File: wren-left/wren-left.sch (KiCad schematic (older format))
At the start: 65 parts, among them J1 TRRS_Jack, SW0 Reset, U1 ProMicro

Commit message: Finish Left-Hand Schematic
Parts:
- added D31, D32, D33, D34, D35, D36, D37, D38, D39, D40, D41, D42, D43, D44: D_Small, Diode_SMD:D_SOD-123, symbol Device:D_Small
- added MX31, MX32, MX33, MX34, MX35, MX36, MX37, MX38, MX39, MX40, MX42, MX43, MX44: MX-NoLED, MX_Only:MX-1U, symbol MX_Alps_Hybrid:MX-NoLED
- added MX41: MX-NoLED, MX_Only:MX-1.5U, symbol MX_Alps_Hybrid:MX-NoLED
- D1, D10, D11, D12, D13, D14, D15, D16, D17, D18, D19, D2, D20, D21, D22, D23, D24, D25, D26, D27, D28, D29, D3, D30, D4, D5, D6, D7, D8, D9: renamed from D?; footprint (none) -> Diode_SMD:D_SOD-123
- J1: footprint (none) -> footprints:TRRS_JACK_MJ4PP9
- MX1, MX10, MX11, MX12, MX13, MX14, MX15, MX16, MX17, MX18, MX19, MX2, MX20, MX21, MX22, MX23, MX24, MX25, MX26, MX27, MX28, MX29, MX3, MX30, MX4, MX5, MX6, MX7, MX8, MX9: renamed from MX?; footprint (none) -> MX_Only:MX-1U
- R1, R2: footprint (none) -> Resistor_SMD:R_0805_2012Metric
- SW0: footprint (none) -> random-keyboard-parts:SKQG-1155865
- U1: footprint (none) -> footprints:ARDUINO_PRO_MICRO
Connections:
- net COL8: now reaches U1.1 (TX(PD3))
- net COL8: now also MX19.1 (COL), MX29.1 (COL), MX9.1 (COL), MX39.1 (COL)
- net ROW3: now reaches U1.10 (D7(PE6))
- net ROW3: now also D31.1 (K), D32.1 (K), D33.1 (K), D34.1 (K), D35.1 (K), D36.1 (K), D37.1 (K), D38.1 (K), D39.1 (K), D40.1 (K)
- net ROW4: now reaches U1.11 (D8(PB4))
- net ROW4: now also D41.1 (K), D42.1 (K), D43.1 (K), D44.1 (K)
- net COL7: now reaches U1.13 (D10(PB6))
- net COL7: now also MX18.1 (COL), MX28.1 (COL), MX8.1 (COL), MX38.1 (COL)
- net COL6: now reaches U1.14 (D16(PB2))
- net COL6: now also MX17.1 (COL), MX27.1 (COL), MX7.1 (COL), MX37.1 (COL)
- net COL5: now reaches U1.15 (D14(PB3))
- net COL5: now also MX16.1 (COL), MX26.1 (COL), MX6.1 (COL), MX36.1 (COL)
- net COL4: now reaches U1.16 (D15(PB1))
- net COL4: now also MX15.1 (COL), MX25.1 (COL), MX5.1 (COL), MX35.1 (COL)
- net COL3: now reaches U1.17 (A0(PF7))
- net COL3: now also MX14.1 (COL), MX24.1 (COL), MX4.1 (COL), MX34.1 (COL), MX44.1 (COL)
- net COL2: now reaches U1.18 (A1(PF6))
- net COL2: now also MX13.1 (COL), MX23.1 (COL), MX3.1 (COL), MX33.1 (COL), MX43.1 (COL)
- net COL1: now reaches U1.19 (A2(PF5))
- net COL1: now also MX12.1 (COL), MX2.1 (COL), MX22.1 (COL), MX32.1 (COL), MX42.1 (COL)
- net COL9: now reaches U1.2 (RX(PD2))
- net COL9: now also MX10.1 (COL), MX20.1 (COL), MX30.1 (COL), MX40.1 (COL)
- net COL0: now reaches U1.20 (A3(PF4))
- net COL0: now also MX1.1 (COL), MX11.1 (COL), MX21.1 (COL), MX31.1 (COL), MX41.1 (COL)
- net ROW0: now reaches U1.7 (D4(PD4))
- net ROW0: now also D1.1 (K), D10.1 (K), D2.1 (K), D3.1 (K), D4.1 (K), D5.1 (K), D6.1 (K), D7.1 (K), D8.1 (K), D9.1 (K)
- net ROW1: now reaches U1.8 (D5(PC6))
- net ROW1: now also D11.1 (K), D12.1 (K), D13.1 (K), D14.1 (K), D15.1 (K), D16.1 (K), D17.1 (K), D18.1 (K), D19.1 (K), D20.1 (K)
- net ROW2: now reaches U1.9 (D6(PD7))
- net ROW2: now also D21.1 (K), D22.1 (K), D23.1 (K), D24.1 (K), D25.1 (K), D26.1 (K), D27.1 (K), D28.1 (K), D29.1 (K), D30.1 (K)
- net at MX1.2 (ROW): now also D1.2 (A)
- net at MX2.2 (ROW): now also D2.2 (A)
- net at D3.2 (A): now also MX3.2 (ROW)
- net at D4.2 (A): now also MX4.2 (ROW)
- net at D5.2 (A): now also MX5.2 (ROW)
- net at D6.2 (A): now also MX6.2 (ROW)
- net at D7.2 (A): now also MX7.2 (ROW)
- net at D8.2 (A): now also MX8.2 (ROW)
- net at D9.2 (A): now also MX9.2 (ROW)
- net at MX10.2 (ROW): now also D10.2 (A)
- net at MX11.2 (ROW): now also D11.2 (A)
- net at MX12.2 (ROW): now also D12.2 (A)
- net at MX13.2 (ROW): now also D13.2 (A)
- net at MX14.2 (ROW): now also D14.2 (A)
- net at MX15.2 (ROW): now also D15.2 (A)
- net at MX16.2 (ROW): now also D16.2 (A)
- net at MX17.2 (ROW): now also D17.2 (A)
- net at MX18.2 (ROW): now also D18.2 (A)
- net at MX19.2 (ROW): now also D19.2 (A)
- net at MX20.2 (ROW): now also D20.2 (A)
- net at MX21.2 (ROW): now also D21.2 (A)
- net at MX22.2 (ROW): now also D22.2 (A)
- net at MX23.2 (ROW): now also D23.2 (A)
- net at MX24.2 (ROW): now also D24.2 (A)
- net at MX25.2 (ROW): now also D25.2 (A)
- net at MX26.2 (ROW): now also D26.2 (A)
- net at MX27.2 (ROW): now also D27.2 (A)
- net at MX28.2 (ROW): now also D28.2 (A)
- net at MX29.2 (ROW): now also D29.2 (A)
- net at MX30.2 (ROW): now also D30.2 (A)
- new net: D31.2 (A), MX31.2 (ROW)
- new net: D32.2 (A), MX32.2 (ROW)
- new net: D33.2 (A), MX33.2 (ROW)
- new net: D34.2 (A), MX34.2 (ROW)
- new net: D35.2 (A), MX35.2 (ROW)
- new net: D36.2 (A), MX36.2 (ROW)
- new net: D37.2 (A), MX37.2 (ROW)
- new net: D38.2 (A), MX38.2 (ROW)
- new net: D39.2 (A), MX39.2 (ROW)
- new net: D40.2 (A), MX40.2 (ROW)
- new net: D41.2 (A), MX41.2 (ROW)
- new net: D42.2 (A), MX42.2 (ROW)
- new net: D43.2 (A), MX43.2 (ROW)
- new net: D44.2 (A), MX44.2 (ROW)
- no-connect marks 0 -> 1
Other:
- moved on the sheet: D1, D10, D11, D12, D13, D14, D15, D16, D17, D18, D19, D2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

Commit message: Routing Half-Finished
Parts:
- J1: footprint footprints:TRRS_JACK_MJ4PP9 -> Connector_Audio:Jack_3.5mm_PJ320E_Horizontal
- MX41: footprint MX_Only:MX-1.5U -> MX_Only:MX-2U-FLIPPED-ReversedStabilizers
- SW0: footprint random-keyboard-parts:SKQG-1155865 -> Button_Switch_THT:SW_PUSH_6mm
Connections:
- net COL0: now also U1.13 (D10(PB6)); no longer U1.20 (A3(PF4))
- net COL1: now also U1.14 (D16(PB2)); no longer U1.19 (A2(PF5))
- net COL2: now also U1.15 (D14(PB3)); no longer U1.18 (A1(PF6))
- net COL3: now also U1.16 (D15(PB1)); no longer U1.17 (A0(PF7))
- net COL4: now also U1.17 (A0(PF7)); no longer U1.16 (D15(PB1))
- net COL5: now also U1.18 (A1(PF6)); no longer U1.15 (D14(PB3))
- net COL6: now also U1.19 (A2(PF5)); no longer U1.14 (D16(PB2))
- net COL7: now also U1.20 (A3(PF4)); no longer U1.13 (D10(PB6))
- net COL8: now also U1.2 (RX(PD2)); no longer U1.1 (TX(PD3))
- net COL9: now also U1.1 (TX(PD3)); no longer U1.2 (RX(PD2))
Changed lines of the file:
@@
 F 0 "J1" H 2607 4675 50  0000 C CNN
 F 1 "TRRS_Jack" H 2607 4584 50  0000 C CNN
-F 2 "footprints:TRRS_JACK_MJ4PP9" H 2650 4350 50  0001 C CNN
+F 2 "Connector_Audio:Jack_3.5mm_PJ320E_Horizontal" H 2650 4350 50  0001 C CNN
 F 3 "~" H 2650 4350 50  0001 C CNN
 	1    2650 4350
@@
 F 0 "SW0" H 3750 3135 50  0000 C CNN
 F 1 "Reset" H 3750 3044 50  0000 C CNN
-F 2 "random-keyboard-parts:SKQG-1155865" H 3750 3050 50  0001 C CNN
+F 2 "Button_Switch_THT:SW_PUSH_6mm" H 3750 3050 50  0001 C CNN
 F 3 "~" H 3750 3050 50  0001 C CNN
 	1    3750 2850
@@
 F 0 "MX41" H 5133 5773 60  0000 C CNN
 F 1 "MX-NoLED" H 5133 5699 20  0000 C CNN
-F 2 "MX_Only:MX-1.5U" H 4475 5525 60  0001 C CNN
+F 2 "MX_Only:MX-2U-FLIPPED-ReversedStabilizers" H 4475 5525 60  0001 C CNN
 F 3 "" H 4475 5525 60  0001 C CNN
 	1    5100 5550
@@
 Text GLabel 9750 2350 1    50   Input ~ 0
 COL9
+Text GLabel 3250 3750 2    50   Input ~ 0
+COL0
+Text GLabel 3250 3650 2    50   Input ~ 0
+COL1
+Text GLabel 3250 3550 2    50   Input ~ 0
+COL2
+Text GLabel 3250 3450 2    50   Input ~ 0
+COL3
+Text GLabel 3250 3350 2    50   Input ~ 0
+COL4
+Text GLabel 3250 3250 2    50   Input ~ 0
+COL5
+Text GLabel 3250 3150 2    50   Input ~ 0
+COL6
 Text GLabel 3250 3050 2    50   Input ~ 0
-COL0
-Text GLabel 3250 3150 2    50   Input ~ 0
-COL1
-Text GLabel 3250 3250 2    50   Input ~ 0
-COL2
-Text GLabel 3250 3350 2    50   Input ~ 0
-COL3
-Text GLabel 3250 3450 2    50   Input ~ 0
-COL4
-Text GLabel 3250 3550 2    50   Input ~ 0
-COL5
-Text GLabel 3250 3650 2    50   Input ~ 0
-COL6
-Text GLabel 3250 3750 2    50   Input ~ 0
 COL7
+Text GLabel 1950 2750 0    50   Input ~ 0
+COL8
 Text GLabel 1950 2650 0    50   Input ~ 0
-COL8
-Text GLabel 1950 2750 0    50   Input ~ 0
 COL9
 Text GLabel 1950 3250 0    50   Input ~ 0

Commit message: Tracks Finished
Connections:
- net COL8: now also U1.9 (D6(PD7)); no longer U1.2 (RX(PD2))
- net COL9: now also U1.10 (D7(PE6)); no longer U1.1 (TX(PD3))
- net ROW0: now also U1.1 (TX(PD3)); no longer U1.7 (D4(PD4))
- net ROW1: now also U1.2 (RX(PD2)); no longer U1.8 (D5(PC6))
- net ROW2: now also U1.7 (D4(PD4)); no longer U1.9 (D6(PD7))
- net ROW3: now also U1.8 (D5(PC6)); no longer U1.10 (D7(PE6))
- net ROW4: now also U1.12 (D9(PB5)); no longer U1.11 (D8(PB4))
- no-connect marks 1 -> 2
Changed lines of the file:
@@
 Text GLabel 1950 3150 0    50   BiDi ~ 0
-SCL
-Text GLabel 3950 4250 2    50   BiDi ~ 0
-SDA
-Text GLabel 3950 4350 2    50   BiDi ~ 0
 SCL
 Text GLabel 3250 2950 2    50   Output ~ 0
@@
 F 3 "~" H 3000 4350 50  0001 C CNN
 	1    3000 4350
-	1    0    0    -1
-$EndComp
-$Comp
-L Device:R_Small R2
-U 1 1 6072E460
-P 3500 4450
-F 0 "R2" H 3559 4496 50  0000 L CNN
-F 1 "10kOhms" H 3559 4405 50  0000 L CNN
-F 2 "Resistor_SMD:R_0805_2012Metric" H 3500 4450 50  0001 C CNN
-F 3 "~" H 3500 4450 50  0001 C CNN
-	1    3500 4450
 	1    0    0    -1
 $EndComp
@@
 Text GLabel 3250 3050 2    50   Input ~ 0
 COL7
+Text GLabel 1950 3450 0    50   Input ~ 0
+COL8
+Text GLabel 1950 3550 0    50   Input ~ 0
+COL9
+Text GLabel 1950 2650 0    50   Input ~ 0
+ROW0
 Text GLabel 1950 2750 0    50   Input ~ 0
-COL8
-Text GLabel 1950 2650 0    50   Input ~ 0
-COL9
+ROW1
 Text GLabel 1950 3250 0    50   Input ~ 0
-ROW0
+ROW2
 Text GLabel 1950 3350 0    50   Input ~ 0
-ROW1
-Text GLabel 1950 3450 0    50   Input ~ 0
-ROW2
-Text GLabel 1950 3550 0    50   Input ~ 0
 ROW3
-Text GLabel 1950 3650 0    50   Input ~ 0
+Text GLabel 1950 3750 0    50   Input ~ 0
 ROW4
-NoConn ~ 1950 3750
+NoConn ~ 1950 3650
+NoConn ~ 1850 4650
+$Comp
+L Device:R_Small R2
+U 1 1 6072E460
+P 3500 4450
+F 0 "R2" H 3559 4496 50  0000 L CNN
+F 1 "10kOhms" H 3559 4405 50  0000 L CNN
+F 2 "Resistor_SMD:R_0805_2012Metric" H 3500 4450 50  0001 C CNN
+F 3 "~" H 3500 4450 50  0001 C CNN
+	1    3500 4450
+	1    0    0    -1
+$EndComp
+Text GLabel 3950 4350 2    50   BiDi ~ 0
+SCL
+Text GLabel 3950 4250 2    50   BiDi ~ 0
+SDA
 $EndSCHEMATC

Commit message: Switch to Elite C Footprints
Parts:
- U1: value ProMicro -> Elite-C; footprint footprints:ARDUINO_PRO_MICRO -> footprints:Elite-C; symbol random-keyboard-parts:ProMicro_2 -> keebio:Elite-C
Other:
- moved on the sheet: SW0
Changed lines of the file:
@@
 $EndComp
 $Comp
-L random-keyboard-parts:ProMicro_2 U1
+L keebio:Elite-C U1
 U 1 1 6071F7CA
-P 2600 3200
-F 0 "U1" H 2600 4015 50  0000 C CNN
-F 1 "ProMicro" H 2600 3924 50  0000 C CNN
-F 2 "footprints:ARDUINO_PRO_MICRO" H 2550 3300 50  0001 C CNN
-F 3 "" H 2550 3300 50  0001 C CNN
-	1    2600 3200
-	1    0    0    -1
-$EndComp
-Text GLabel 1950 3050 0    50   BiDi ~ 0
+P 2500 2000
+F 0 "U1" H 2500 2815 50  0000 C CNN
+F 1 "Elite-C" H 2500 2724 50  0000 C CNN
+F 2 "footprints:Elite-C" H 2450 2100 50  0001 C CNN
+F 3 "" H 2450 2100 50  0001 C CNN
+	1    2500 2000
+	1    0    0    -1
+$EndComp
+Text GLabel 1800 1850 0    50   BiDi ~ 0
 SDA
-Text GLabel 1950 3150 0    50   BiDi ~ 0
+Text GLabel 1800 1950 0    50   BiDi ~ 0
 SCL
-Text GLabel 3250 2950 2    50   Output ~ 0
+Text GLabel 3200 1750 2    50   Output ~ 0
 VCC
 Text GLabel 3950 4550 2    50   Input ~ 0
@@
 Text GLabel 2850 4550 2    50   Output ~ 0
 GND
-Text GLabel 3250 2750 2    50   Input ~ 0
+Text GLabel 3200 1550 2    50   Input ~ 0
 GND
 $Comp
@@
 L Switch:SW_Push SW0
 U 1 1 60738E12
-P 3750 2850
-F 0 "SW0" H 3750 3135 50  0000 C CNN
-F 1 "Reset" H 3750 3044 50  0000 C CNN
-F 2 "Button_Switch_THT:SW_PUSH_6mm" H 3750 3050 50  0001 C CNN
-F 3 "~" H 3750 3050 50  0001 C CNN
-	1    3750 2850
-	1    0    0    -1
-$EndComp
-Wire Wire Line
-	3250 2850 3550 2850
-Text GLabel 3950 2850 2    50   Output ~ 0
+P 3700 1650
+F 0 "SW0" H 3700 1935 50  0000 C CNN
+F 1 "Reset" H 3700 1844 50  0000 C CNN
+F 2 "Button_Switch_THT:SW_PUSH_6mm" H 3700 1850 50  0001 C CNN
+F 3 "~" H 3700 1850 50  0001 C CNN
+	1    3700 1650
+	1    0    0    -1
+$EndComp
+Wire Wire Line
+	3200 1650 3500 1650
+Text GLabel 3900 1650 2    50   Output ~ 0
 GND
 $Comp
@@
 Text GLabel 9750 2350 1    50   Input ~ 0
 COL9
-Text GLabel 3250 3750 2    50   Input ~ 0
+Text GLabel 3200 2550 2    50   Input ~ 0
 COL0
-Text GLabel 3250 3650 2    50   Input ~ 0
+Text GLabel 3200 2450 2    50   Input ~ 0
 COL1
-Text GLabel 3250 3550 2    50   Input ~ 0
+Text GLabel 3200 2350 2    50   Input ~ 0
 COL2
-Text GLabel 3250 3450 2    50   Input ~ 0
+Text GLabel 3200 2250 2    50   Input ~ 0
 COL3
-Text GLabel 3250 3350 2    50   Input ~ 0
+Text GLabel 3200 2150 2    50   Input ~ 0
 COL4
-Text GLabel 3250 3250 2    50   Input ~ 0
+Text GLabel 3200 2050 2    50   Input ~ 0
 COL5
-Text GLabel 3250 3150 2    50   Input ~ 0
+Text GLabel 3200 1950 2    50   Input ~ 0
 COL6
-Text GLabel 3250 3050 2    50   Input ~ 0
+Text GLabel 3200 1850 2    50   Input ~ 0
 COL7
-Text GLabel 1950 3450 0    50   Input ~ 0
+Text GLabel 1800 2250 0    50   Input ~ 0
 COL8
-Text GLabel 1950 3550 0    50   Input ~ 0
+Text GLabel 1800 2350 0    50   Input ~ 0
 COL9
-Text GLabel 1950 2650 0    50   Input ~ 0
+Text GLabel 1800 1450 0    50   Input ~ 0
 ROW0
-Text GLabel 1950 2750 0    50   Input ~ 0
+Text GLabel 1800 1550 0    50   Input ~ 0
 ROW1
-Text GLabel 1950 3250 0    50   Input ~ 0
+Text GLabel 1800 2050 0    50   Input ~ 0
 ROW2
-Text GLabel 1950 3350 0    50   Input ~ 0
+Text GLabel 1800 2150 0    50   Input ~ 0
 ROW3
-Text GLabel 1950 3750 0    50   Input ~ 0
+Text GLabel 1800 2550 0    50   Input ~ 0
 ROW4
-NoConn ~ 1950 3650
+NoConn ~ 1800 2450
 NoConn ~ 1850 4650
 $Comp
@@
 Text GLabel 3950 4250 2    50   BiDi ~ 0
 SDA
+Text GLabel 1600 1650 2    50   Output ~ 0
+GND
+Text GLabel 1600 1750 2    50   Output ~ 0
+GND
 $EndSCHEMATC

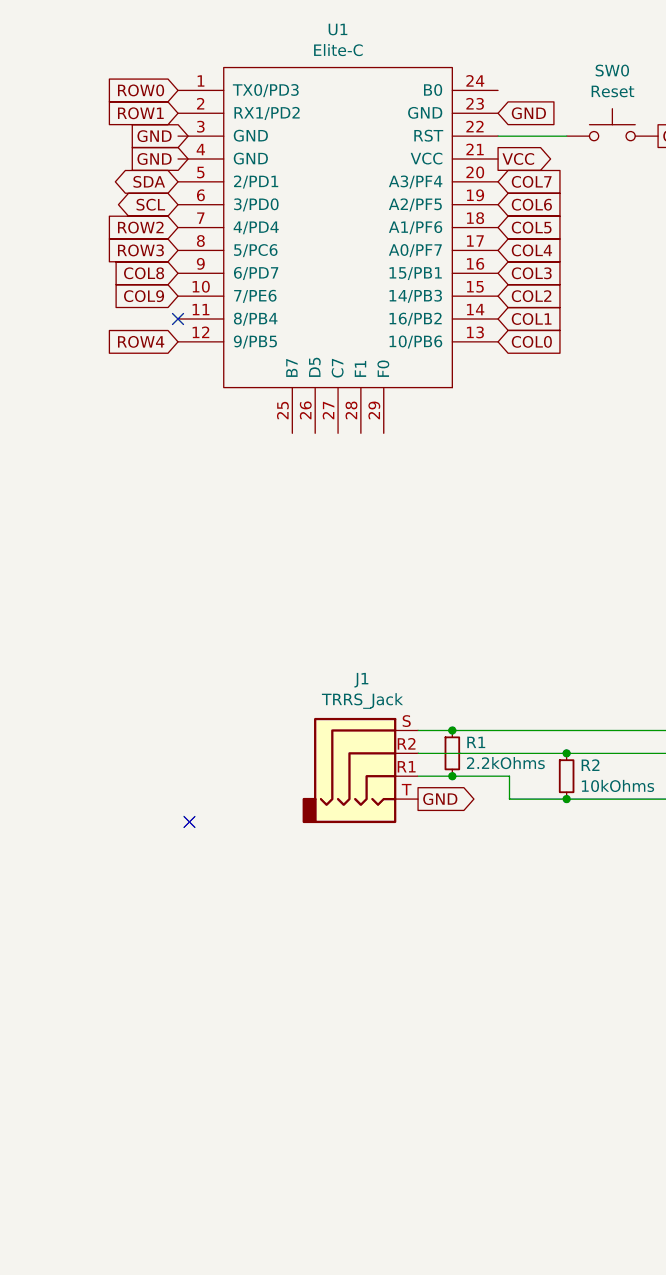
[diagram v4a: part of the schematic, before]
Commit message: Add Encoders to PCB
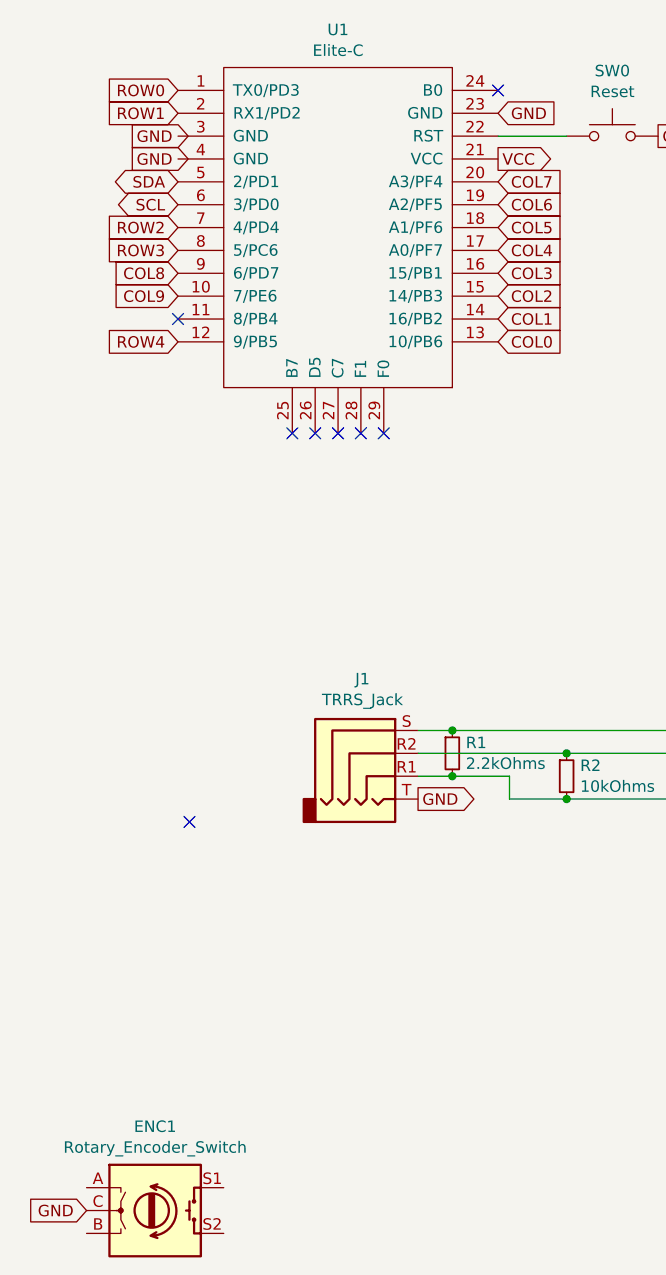
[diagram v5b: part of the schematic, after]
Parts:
- added ENC1: Rotary_Encoder_Switch, Rotary_Encoder:RotaryEncoder_Alps_EC11E-Switch_Vertical_H20mm, symbol Device:Rotary_Encoder_Switch
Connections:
- net GND: now also ENC1.C
- no-connect marks 2 -> 8
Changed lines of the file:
@@
 Text GLabel 1600 1750 2    50   Output ~ 0
 GND
+NoConn ~ 3200 1450
+NoConn ~ 2300 2950
+NoConn ~ 2400 2950
+NoConn ~ 2500 2950
+NoConn ~ 2600 2950
+NoConn ~ 2700 2950
+$Comp
+L Device:Rotary_Encoder_Switch ENC1
+U 1 1 60759DC4
+P 1700 6350
+F 0 "ENC1" H 1700 6717 50  0000 C CNN
+F 1 "Rotary_Encoder_Switch" H 1700 6626 50  0000 C CNN
+F 2 "Rotary_Encoder:RotaryEncoder_Alps_EC11E-Switch_Vertical_H20mm" H 1550 6510 50  0001 C CNN
+F 3 "~" H 1700 6610 50  0001 C CNN
+	1    1700 6350
+	1    0    0    -1
+$EndComp
+Text GLabel 1400 6350 0    50   Input ~ 0
+GND
 $EndSCHEMATC

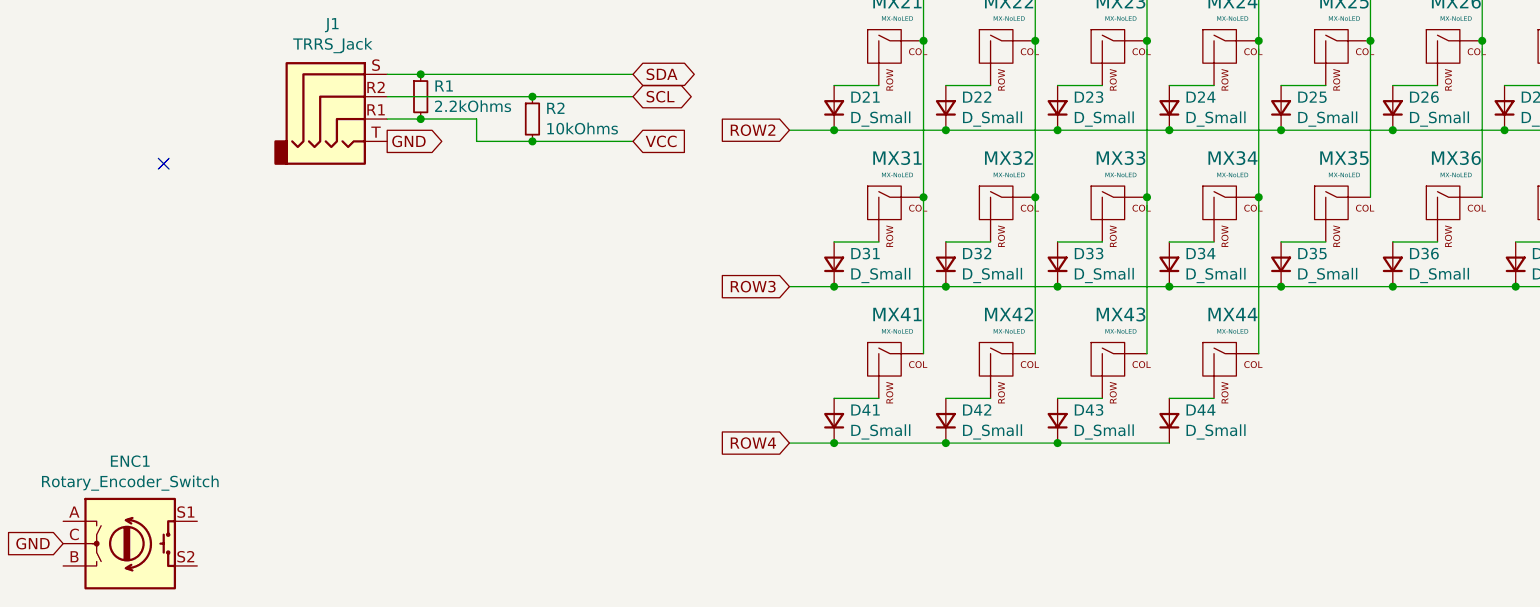
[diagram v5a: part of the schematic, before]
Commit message: Component Updates
Switch to through-hole diodes and resistors, reroute traces, etc.
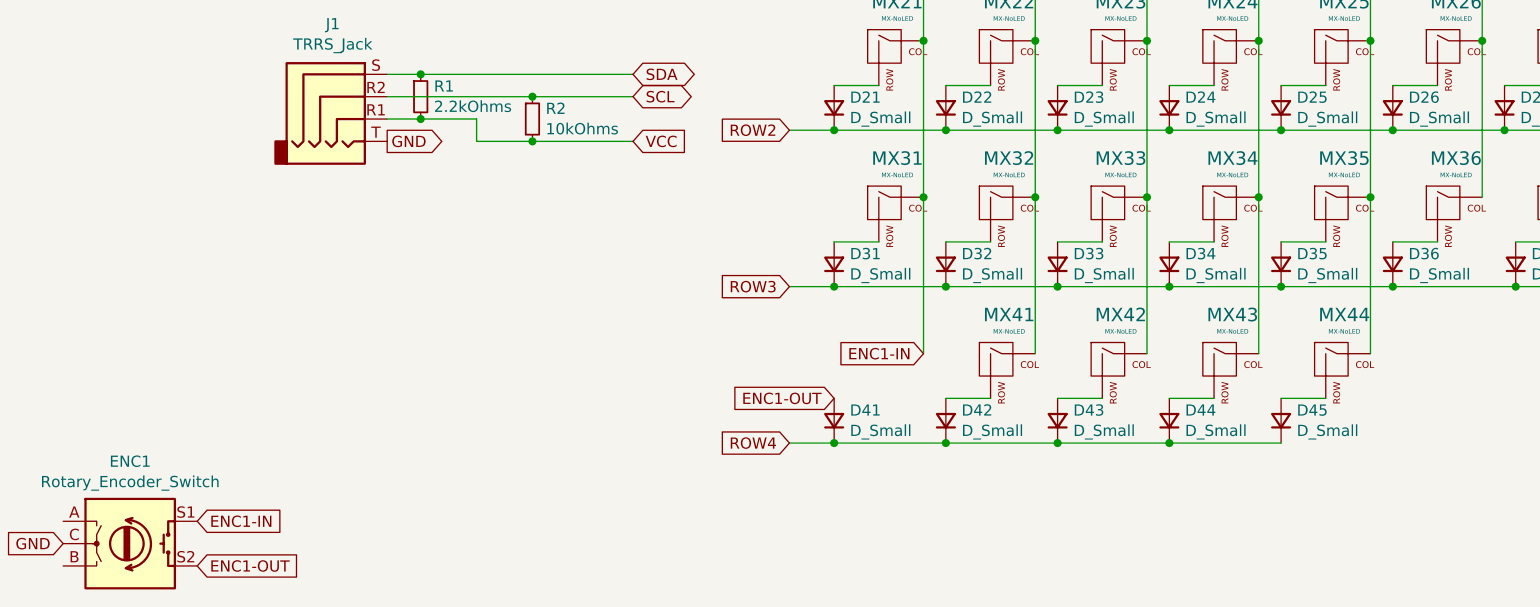
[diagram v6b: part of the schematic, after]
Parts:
- added D41: D_Small, footprints:D_SOD123_axial, symbol Device:D_Small
- D1, D10, D11, D12, D13, D14, D15, D16, D17, D18, D19, D2, D20, D21, D22, D23, D24, D25, D26, D27, D28, D29, D3, D30, D31, D32, D33, D34, D35, D36, D37, D38, D39, D4, D40, D5, D6, D7, D8, D9: footprint Diode_SMD:D_SOD-123 -> footprints:D_SOD123_axial
- D42: renamed from D41; footprint Diode_SMD:D_SOD-123 -> footprints:D_SOD123_axial
- D43: renamed from D42; footprint Diode_SMD:D_SOD-123 -> footprints:D_SOD123_axial
- D44: renamed from D43; footprint Diode_SMD:D_SOD-123 -> footprints:D_SOD123_axial
- D45: renamed from D44; footprint Diode_SMD:D_SOD-123 -> footprints:D_SOD123_axial
- R1, R2: footprint Resistor_SMD:R_0805_2012Metric -> Resistor_THT:R_Axial_DIN0204_L3.6mm_D1.6mm_P1.90mm_Vertical
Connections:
- net COL0: now also ENC1.S1; no longer MX41.1 (COL)
- net COL1: now also MX41.1 (COL); no longer MX42.1 (COL)
- net COL2: now also MX42.1 (COL); no longer MX43.1 (COL)
- net COL3: now also MX43.1 (COL); no longer MX44.1 (COL)
- net COL4: now also MX44.1 (COL)
- net ROW4: now also D41.1 (K)
- net ENC1-OUT: now reaches ENC1.S2
- net ENC1-OUT: now also D41.2 (A)
- no-connect marks 8 -> 7
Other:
- moved on the sheet: D42, D43, D44, D45, MX41, MX42, MX43, MX44
